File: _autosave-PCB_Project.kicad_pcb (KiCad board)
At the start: 8 copper layers, 152.4 x 101.6 mm, 169 parts, among them J1 Picoblade_CFG, J2 DF9-41P-1V32, J3 DF9-CFG-SPW1, Q1 SOC2222AHRG, Q2 SOC2222AHRG, U1 NX1H35 PBGA625, U10 MAX8556ETE, U11 AS4C8M16SA-6TIN, U2 CY15B108QN-40SXI, U3 CY15B108QN-40SXI, U4 CY15B108QN-40SXI, U5 AS4C8M32S-6TIN, U6 M95P32-IXMNT/E, U7 TPS3828-33DBVR, U8 MAX8556ETE, U9 MAX8556ETE, Y2 LFSPXO025225_25MHz

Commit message: full components, LEDS, changed edges
all components on pcb editor. added and  routed leds and 2 PLL. changed edges o have more space
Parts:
- moved U11 5.91 mm to (87.3, 101.3)
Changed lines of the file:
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@@
 	(footprint "DataHub_Footprints:sdram2_TSOP-54_11P96X22P35_ALL"
 		(layer "B.Cu")
-		(at 91.8011 97.491241 -90)
+		(at 87.3011 101.316039 -90)
 		(tags "AS4C8M16SA-6TIN ")
 		(property "Reference" "U11"

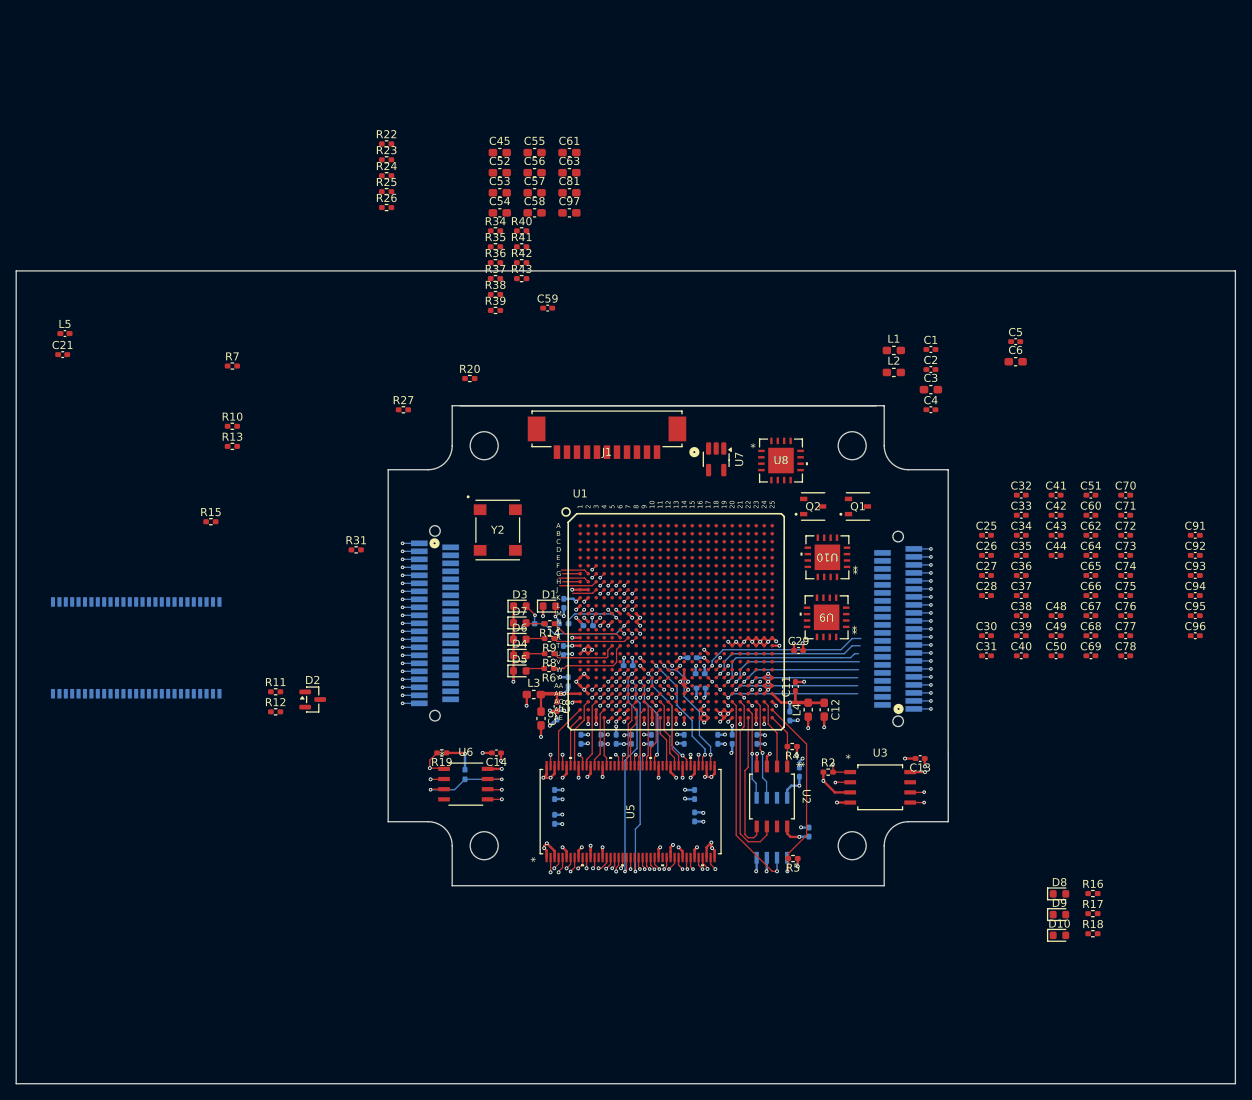
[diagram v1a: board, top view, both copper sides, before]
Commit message: SPW Bank0
completed SPW, rotated edges and adjusted dimensions to make the extra sdram bga fit. completed Bank 0 (still to route to connector). Started fanout of bga sdram
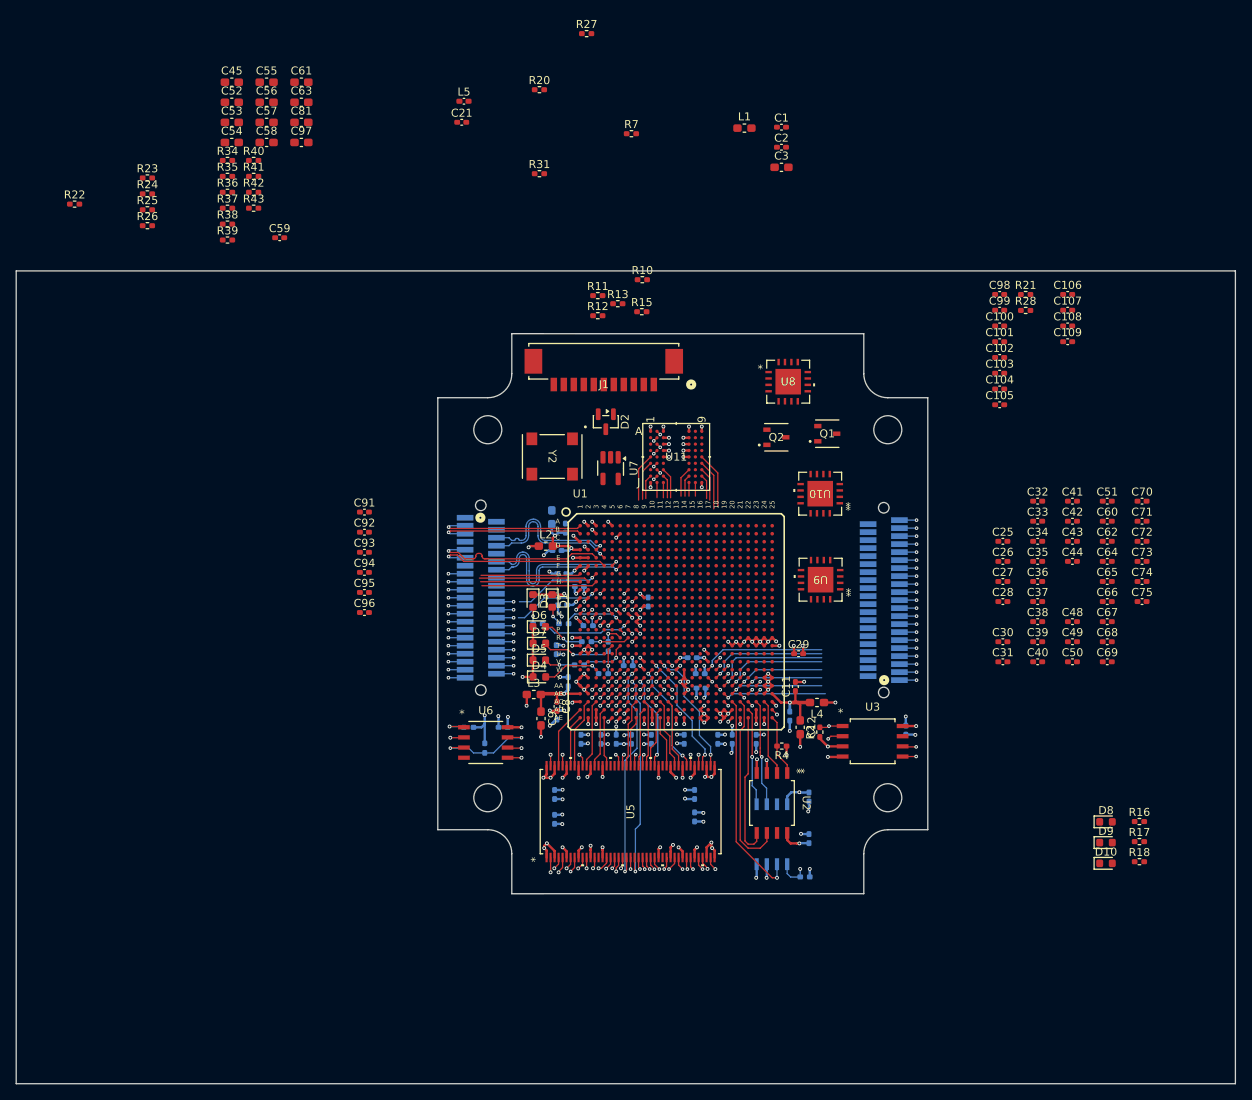
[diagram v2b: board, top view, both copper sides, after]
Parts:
- added C100: 22nF, Capacitor_SMD:C_0402_1005Metric_Pad0.74x0.62mm_HandSolder, F.Cu at (195.2, 61.1)
- added C101: 22nF, Capacitor_SMD:C_0402_1005Metric_Pad0.74x0.62mm_HandSolder, F.Cu at (195.2, 63.1)
- added C102: 100nF, Capacitor_SMD:C_0402_1005Metric_Pad0.74x0.62mm_HandSolder, F.Cu at (195.2, 65.0)
- added C103: 100nF, Capacitor_SMD:C_0402_1005Metric_Pad0.74x0.62mm_HandSolder, F.Cu at (195.2, 67.0)
- added C104: 22nF, Capacitor_SMD:C_0402_1005Metric_Pad0.74x0.62mm_HandSolder, F.Cu at (195.2, 69.0)
- added C105: 22nF, Capacitor_SMD:C_0402_1005Metric_Pad0.74x0.62mm_HandSolder, F.Cu at (195.2, 70.9)
- added C106: 100nF, Capacitor_SMD:C_0402_1005Metric_Pad0.74x0.62mm_HandSolder, F.Cu at (203.7, 57.1)
- added C107: 100nF, Capacitor_SMD:C_0402_1005Metric_Pad0.74x0.62mm_HandSolder, F.Cu at (203.7, 59.1)
- added C108: 100nF, Capacitor_SMD:C_0402_1005Metric_Pad0.74x0.62mm_HandSolder, F.Cu at (203.7, 61.1)
- added C109: 100nF, Capacitor_SMD:C_0402_1005Metric_Pad0.74x0.62mm_HandSolder, F.Cu at (203.7, 63.1)
- added C98: 100nF, Capacitor_SMD:C_0402_1005Metric_Pad0.74x0.62mm_HandSolder, F.Cu at (195.2, 57.1)
- added C99: 100nF, Capacitor_SMD:C_0402_1005Metric_Pad0.74x0.62mm_HandSolder, F.Cu at (195.2, 59.1)
- added R21: 0 Ohm, Resistor_SMD:R_0402_1005Metric_Pad0.72x0.64mm_HandSolder, F.Cu at (198.5, 57.2)
- added R28: 0 Ohm, Resistor_SMD:R_0402_1005Metric_Pad0.72x0.64mm_HandSolder, F.Cu at (198.5, 59.1)
- C13, C14, C4, C5, C6, C76, C77, C78, R14, R19, R5, R6, R8, R9: moved to B.Cu
- U11: value AS4C8M16SA-6TIN -> AS4C8M16S-6BIN; footprint DataHub_Footprints:sdram2_TSOP-54_11P96X22P35_ALL -> DataHub_Footprints:sdram2_bga_TFBGA-54_8X8_ALL; moved to F.Cu
- moved C91 103.9 mm to (115.8, 84.4)
- moved C92 103.9 mm to (115.8, 86.9)
- moved C93 103.9 mm to (115.8, 89.4)
- moved C94 103.9 mm to (115.8, 91.9)
- moved C95 103.9 mm to (115.8, 94.4)
- moved C96 103.9 mm to (115.8, 96.9)
- moved U11 71.6 mm to (154.8, 77.5), turned to 0 degrees
- moved C76 70.7 mm to (140.5, 92.1), turned to 180 degrees
- moved C77 68.6 mm to (142.7, 93.7)
- moved R11 63.8 mm to (145.0, 57.3)
- moved R12 63.8 mm to (145.0, 59.8)
- moved C6 61.2 mm to (139.3, 85.0), turned to 90 degrees
- moved C5 60.9 mm to (141.0, 86.4), turned to 90 degrees
- moved C78 60.1 mm to (151.3, 95.6), turned to 90 degrees
- moved R15 59.9 mm to (150.5, 59.3)
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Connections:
- J3 pad 1: unconnected-(J3-Pad1) -> GND
- J3 pad 10: unconnected-(J3-Pad10) -> GND
- J3 pad 11: unconnected-(J3-Pad11) -> /02_FPGA_Config_JTAG_Bitstream_Reset/SPW1_DOUT_N
- J3 pad 12: unconnected-(J3-Pad12) -> /02_FPGA_Config_JTAG_Bitstream_Reset/SPW1_SOUT_P
- J3 pad 13: unconnected-(J3-Pad13) -> GND
- J3 pad 14: unconnected-(J3-Pad14) -> /02_FPGA_Config_JTAG_Bitstream_Reset/SPW1_SOUT_N
- J3 pad 2: unconnected-(J3-Pad2) -> GND
- J3 pad 29: GND -> unconnected-(J3-Pad29)
- J3 pad 3: unconnected-(J3-Pad3) -> /02_FPGA_Config_JTAG_Bitstream_Reset/SPW1_SIN_P
- J3 pad 30: /02_FPGA_Config_JTAG_Bitstream_Reset/SPW1_DIN_P -> unconnected-(J3-Pad30)
- J3 pad 31: /02_FPGA_Config_JTAG_Bitstream_Reset/SPW1_SOUT_P -> unconnected-(J3-Pad31)
- J3 pad 32: /02_FPGA_Config_JTAG_Bitstream_Reset/SPW1_DIN_N -> unconnected-(J3-Pad32)
- J3 pad 33: /02_FPGA_Config_JTAG_Bitstream_Reset/SPW1_SOUT_N -> unconnected-(J3-Pad33)
- J3 pad 34: GND -> unconnected-(J3-Pad34)
- J3 pad 35: GND -> unconnected-(J3-Pad35)
- J3 pad 36: /02_FPGA_Config_JTAG_Bitstream_Reset/SPW1_SIN_P -> unconnected-(J3-Pad36)
- J3 pad 37: /02_FPGA_Config_JTAG_Bitstream_Reset/SPW1_DOUT_P -> unconnected-(J3-Pad37)
- J3 pad 38: /02_FPGA_Config_JTAG_Bitstream_Reset/SPW1_SIN_N -> unconnected-(J3-Pad38)
- J3 pad 39: /02_FPGA_Config_JTAG_Bitstream_Reset/SPW1_DOUT_N -> unconnected-(J3-Pad39)
- J3 pad 4: unconnected-(J3-Pad4) -> GND
- J3 pad 40: GND -> unconnected-(J3-Pad40)
- J3 pad 41: GND -> unconnected-(J3-Pad41)
- J3 pad 5: unconnected-(J3-Pad5) -> /02_FPGA_Config_JTAG_Bitstream_Reset/SPW1_SIN_N
- J3 pad 6: unconnected-(J3-Pad6) -> /02_FPGA_Config_JTAG_Bitstream_Reset/SPW1_DIN_P
- J3 pad 7: unconnected-(J3-Pad7) -> GND
- J3 pad 8: unconnected-(J3-Pad8) -> /02_FPGA_Config_JTAG_Bitstream_Reset/SPW1_DIN_N
- J3 pad 9: unconnected-(J3-Pad9) -> /02_FPGA_Config_JTAG_Bitstream_Reset/SPW1_DOUT_P
- U1 pad A12: GND -> unconnected-(U1F-VTO_11-PadA12)
- U1 pad A15: GND -> VDDIO_10
- U1 pad A17: unconnected-(U1B-IO_B10D12N_DQ_SWDO-PadA17) -> /07_IO_DF9_connectors/SDRAM_B_A10
- U1 pad A18: unconnected-(U1B-IO_B10D12P_DQ_SWDO-PadA18) -> /07_IO_DF9_connectors/SDRAM_B_WE_N
- U1 pad A9: GND -> VDDIO_11
- U1 pad B13: GND -> VDDIO_10
- U1 pad B14: GND -> unconnected-(U1B-VTO_10-PadB14)
- U1 pad B18: GND -> unconnected-(U1B-VTO_10-PadB18)
- U1 pad B19: GND -> VDDIO_10
- U1 pad B7: GND -> VDDIO_11
- U1 pad B8: GND -> unconnected-(U1F-VTO_11-PadB8)
- U1 pad C17: unconnected-(U1B-IO_B10D07N-PadC17) -> /07_IO_DF9_connectors/SDRAM_B_CS_N
- U1 pad C18: unconnected-(U1B-IO_B10D13P_DQS_SWSO-PadC18) -> /07_IO_DF9_connectors/SDRAM_B_DQ7
- U1 pad D12: GND -> VDDIO_11
- U1 pad F12: GND -> VDDIO_11
- U1 pad H13: GND -> VDDIO_10
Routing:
- net unconnected-(U1A-IO_B0D10N-PadJ8): track 23.7 -> 0.00 mm, vias 1 -> 0
- net unconnected-(U1A-IO_B0D03N-PadJ6): track 23.2 -> 0.00 mm, vias 1 -> 0
- net unconnected-(U1A-IO_B0D02P-PadJ3): track 3.09 -> 24.1 mm, vias 0 -> 1
- net unconnected-(U1A-IO_B0D03P-PadJ5): track 20.3 -> 0.00 mm, vias 1 -> 0
- net /02_FPGA_Config_JTAG_Bitstream_Reset/SPW1_DOUT_N: track 2.15 -> 22.3 mm
- net /02_FPGA_Config_JTAG_Bitstream_Reset/SPW1_DOUT_P: track 2.15 -> 22.2 mm
- net /02_FPGA_Config_JTAG_Bitstream_Reset/SPW1_SOUT_P: track 2.15 -> 22.1 mm
- net /02_FPGA_Config_JTAG_Bitstream_Reset/SPW1_SOUT_N: track 2.15 -> 22.1 mm
- net /02_FPGA_Config_JTAG_Bitstream_Reset/SPW1_SIN_N: track 0.00 -> 19.2 mm, vias 0 -> 1
- net /02_FPGA_Config_JTAG_Bitstream_Reset/SPW1_SIN_P: track 0.00 -> 19.2 mm, vias 0 -> 1
- net /02_FPGA_Config_JTAG_Bitstream_Reset/SPW1_DIN_N: track 0.00 -> 18.3 mm, vias 0 -> 1
- net /02_FPGA_Config_JTAG_Bitstream_Reset/SPW1_DIN_P: track 0.00 -> 18.3 mm, vias 0 -> 1
- net unconnected-(U1D-IO_B5D12N_DQ_SWDO-PadV18): track 24.0 -> 13.0 mm
- net unconnected-(U1D-IO_B5D12P_DQ_SWDO-PadW18): track 24.2 -> 13.2 mm
- net unconnected-(U1D-IO_B5D11N_DQ-PadW19): track 23.0 -> 12.3 mm
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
